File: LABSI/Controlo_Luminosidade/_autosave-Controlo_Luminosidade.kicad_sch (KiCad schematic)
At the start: 45 parts, among them J1 Barrel_Jack_Switch, J10 Touch Button, J11 Touch Button, J12 Touch Button, J2 Barrel_Jack_Switch, J3 Conn_01x05_Pin, J4 Conn_01x04_Pin, J5 Conn_01x04_Pin, J6 AVR-ISP-6, J7 Conn_01x03_Pin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

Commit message: sonar not working, integration with esp32 iot,
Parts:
- added J13: ESP32, symbol Connector_Generic:Conn_01x04
- added R8: 670, symbol Device:R
- added R9: 1k, symbol Device:R
- R2: value 330 -> 220
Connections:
- net +5V: now also J13.3 (Pin_3)
- net GND: now also J13.4 (Pin_4), R9.2
- net TRIG: now also U1.25 (PC2); no longer U1.2 (PD0)
- net TRIG2: now also U1.26 (PC3); no longer U1.3 (PD1)
- new net ESP32/TX: J13.2 (Pin_2), R8.2, R9.1
- new net RX/TX_ESP: J13.1 (Pin_1), U1.2 (PD0)
- new net TX: R8.1, U1.3 (PD1)
- no-connect marks 8 -> 6
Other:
- moved on the sheet: J10

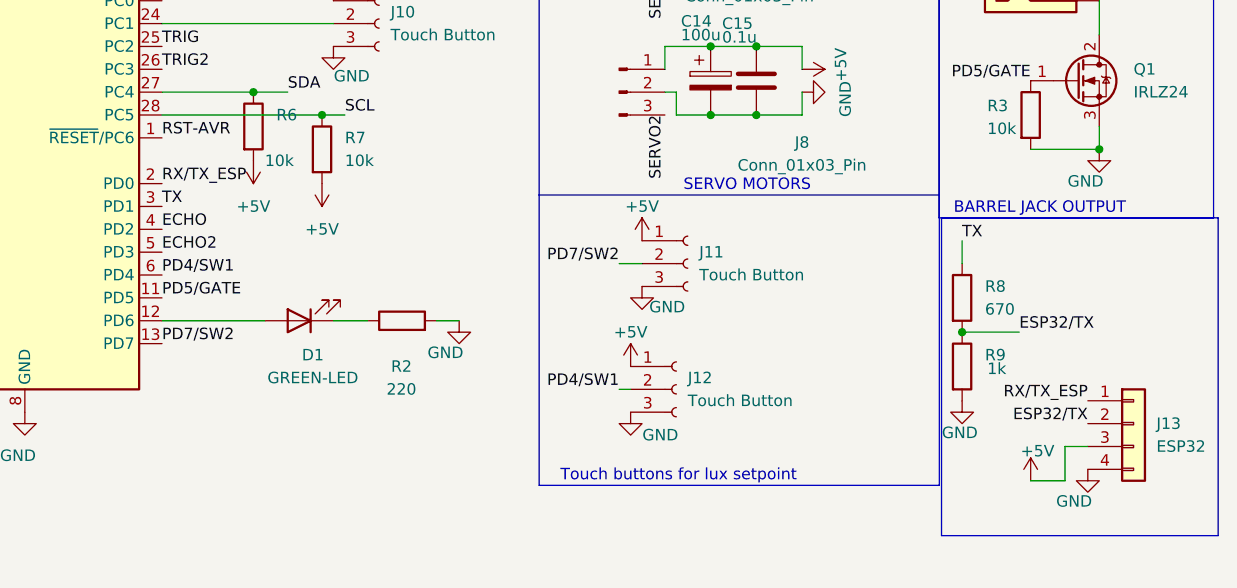
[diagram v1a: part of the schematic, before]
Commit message: controlo web funcional. falta adicionar controlo da fita led entre mudanças de estado; adicionar oc1b com o segundo motor; limitar duty cycle da fita a 80%; criar botao web para desligar fita; adicionar modo de temporização na ação dos motores
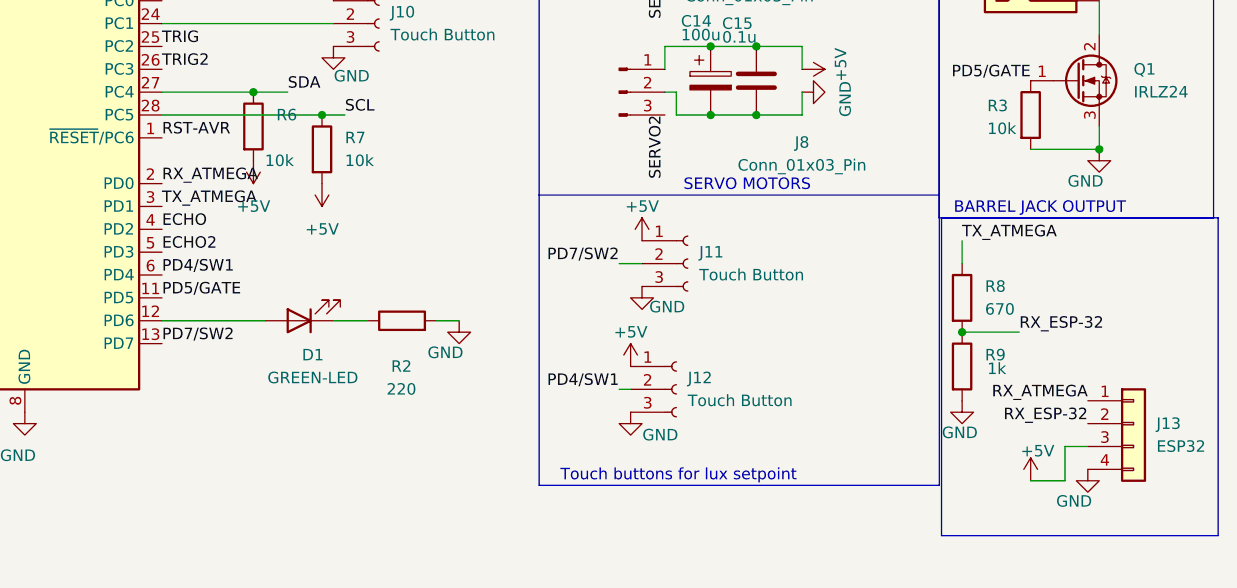
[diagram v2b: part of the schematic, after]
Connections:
- net ESP32/TX renamed RX_ESP-32
- net RX/TX_ESP renamed RX_ATMEGA
- net TX renamed TX_ATMEGA
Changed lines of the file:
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@@
-		)
-	)
-	(label "ESP32{slash}TX"
-		(at 270.51 134.62 180)
-		(effects
-			(font
-				(size 1.27 1.27)
-			)
-			(justify right bottom)
 		)
 	)
@@
 		)
 	)
-	(label "TX"
+	(label "TX_ATMEGA"
 		(at 256.54 114.3 0)
 		(effects
@@
 		)
 	)
-	(label "RX{slash}TX_ESP"
-		(at 270.51 132.08 180)
+	(label "RX_ESP-32"
+		(at 270.51 134.62 180)
 		(effects
 			(font
@@
 		)
 	)
-	(label "RX{slash}TX_ESP"
+	(label "RX_ATMEGA"
 		(at 167.64 107.95 0)
 		(effects
@@
 		)
 	)
-	(label "ESP32{slash}TX"
+	(label "RX_ESP-32"
 		(at 262.89 124.46 0)
 		(effects
@@
 			)
 			(justify left bottom)
+		)
+	)
+	(label "RX_ATMEGA"
+		(at 270.51 132.08 180)
+		(effects
+			(font
+				(size 1.27 1.27)
+			)
+			(justify right bottom)
 		)
 	)
@@
 		)
 	)
-	(label "TX"
+	(label "TX_ATMEGA"
 		(at 167.64 110.49 0)
 		(effects
